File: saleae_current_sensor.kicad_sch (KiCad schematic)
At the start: 35 parts, among them J1 USB4505-03-0-A_REVA, J2 Conn_01x01_Female, J3 Conn_01x01_Female, J4 Conn_02x04_Counter_Clockwise, U1 TES_1-0523, U2 L78L12, U3 L7912, U4 ACS723xLCTR-05AB, U5 ACS723xLCTR-40AB, U6 AD8422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

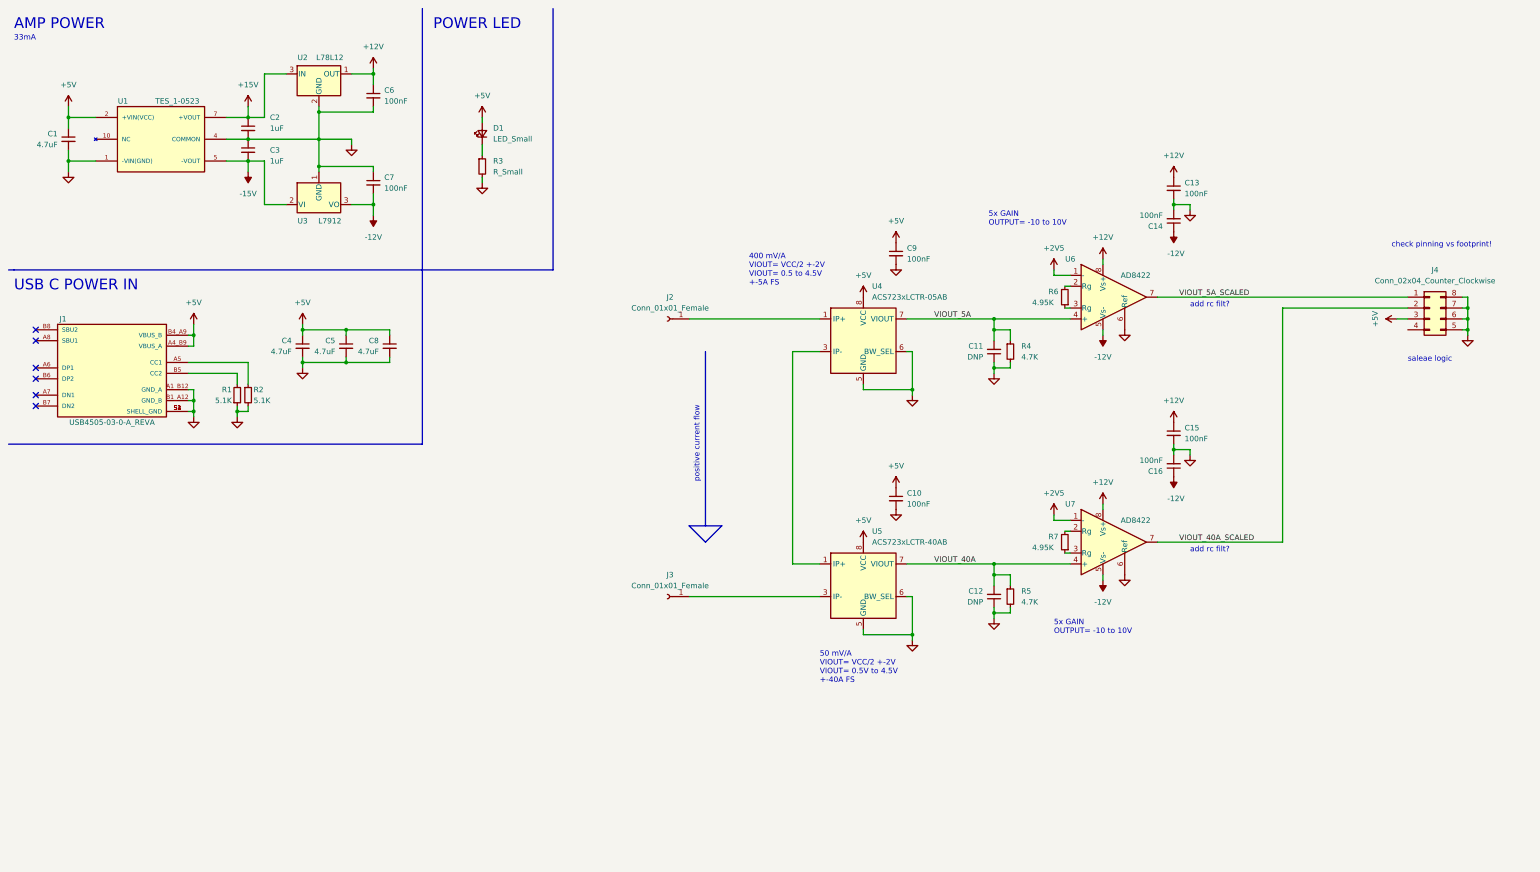
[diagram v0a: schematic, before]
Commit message: Add buffers to raw signals Add connections for main power lines Annotate all components Assign all footprints
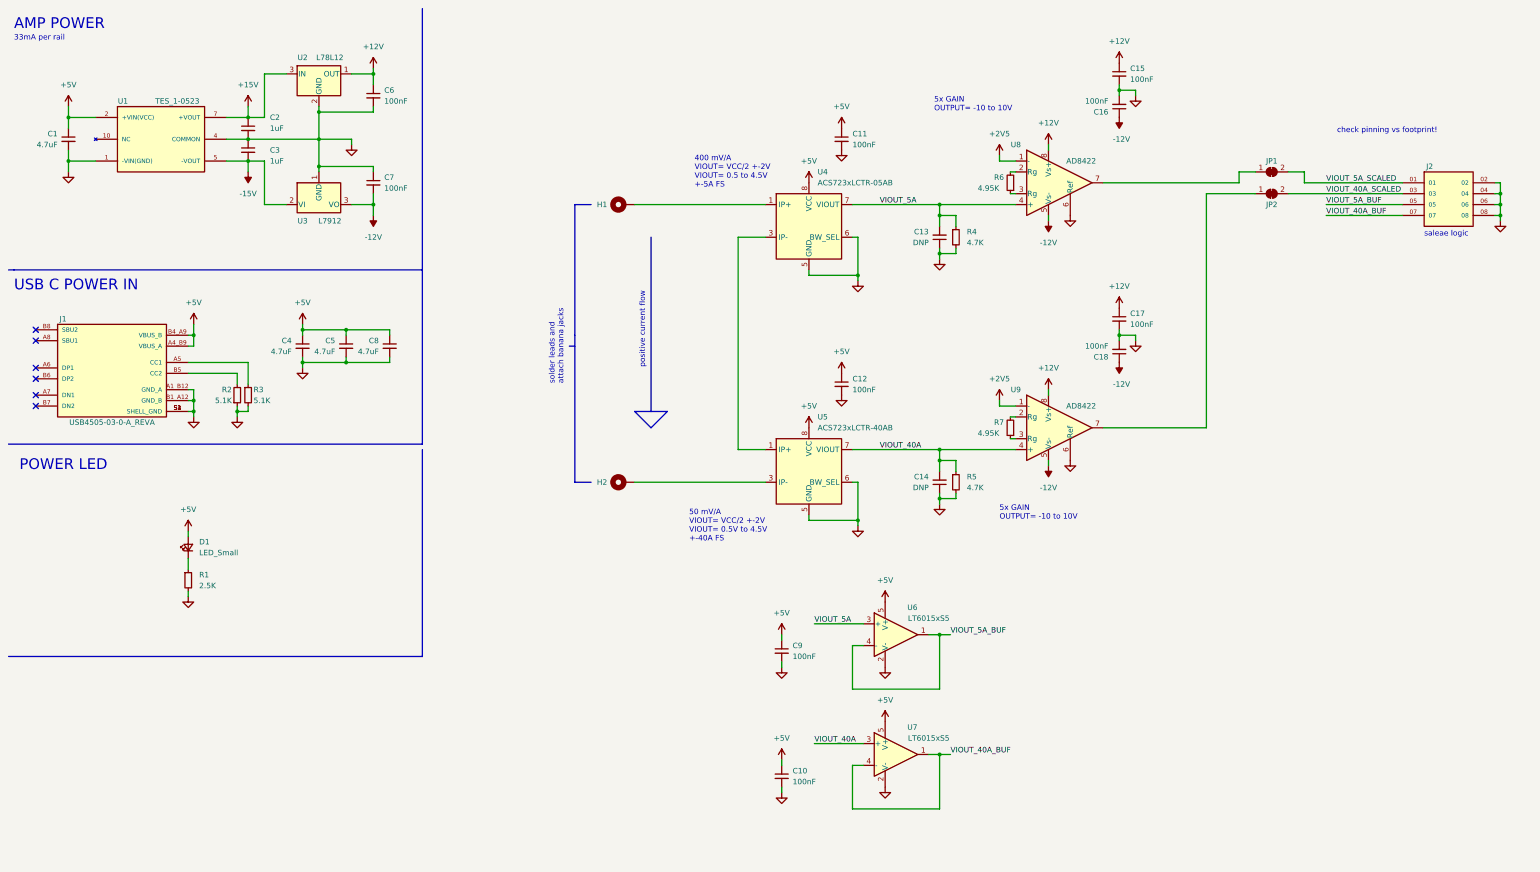
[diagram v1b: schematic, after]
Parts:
- removed J2, J3: Conn_01x01_Female, symbol Connector:Conn_01x01_Female
- removed J4: Conn_02x04_Counter_Clockwise, symbol Connector_Generic:Conn_02x04_Counter_Clockwise
- removed R3: R_Small, symbol Device:R_Small
- added C10, C9: 100nF, Capacitor_SMD:C_0603_1608Metric, symbol Device:C_Small
- added H1: IP, MountingHole:MountingHole_2.7mm_M2.5_ISO7380_Pad_TopBottom, symbol Mechanical:MountingHole_Pad
- added H2: IN, MountingHole:MountingHole_2.7mm_M2.5_ISO7380_Pad_TopBottom, symbol Mechanical:MountingHole_Pad
- added J2: FTSH-104-01-SM-D-RA, FTSH-104-01-SM-D-RA:SAMTEC_FTSH-104-01-SM-D-RA, symbol FTSH-104-01-SM-D-RA:FTSH-104-01-SM-D-RA
- added JP1, JP2: SolderJumper_2_Bridged, Jumper:SolderJumper-2_P1.3mm_Bridged2Bar_Pad1.0x1.5mm, symbol Jumper:SolderJumper_2_Bridged
- added R1: 2.5K, Resistor_SMD:R_0603_1608Metric, symbol Device:R_Small
- added U6, U7: LT6015xS5, Package_TO_SOT_SMD:SOT-23-5, symbol Amplifier_Operational:LT6015xS5
- C1, C2, C3, C4, C5, C8: footprint (none) -> Capacitor_SMD:C_1206_3216Metric
- C11: renamed from C9; footprint (none) -> Capacitor_SMD:C_0603_1608Metric
- C12: renamed from C10; footprint (none) -> Capacitor_SMD:C_0603_1608Metric
- C13: renamed from C11; footprint (none) -> Capacitor_SMD:C_0603_1608Metric
- C14: renamed from C12; footprint (none) -> Capacitor_SMD:C_0603_1608Metric
- C15: renamed from C13; footprint (none) -> Capacitor_SMD:C_0603_1608Metric
- C16: renamed from C14; footprint (none) -> Capacitor_SMD:C_0603_1608Metric
- C17: renamed from C15; footprint (none) -> Capacitor_SMD:C_0603_1608Metric
- C18: renamed from C16; footprint (none) -> Capacitor_SMD:C_0603_1608Metric
- C6, C7: footprint (none) -> Capacitor_SMD:C_0603_1608Metric
- D1: footprint (none) -> LED_SMD:LED_1206_3216Metric
- J1: footprint GCT_USB4505-03-0-A_REVA -> USB4505-03-0-A_REVA:GCT_USB4505-03-0-A_REVA
- R2: renamed from R1; footprint (none) -> Resistor_SMD:R_0603_1608Metric
- R3: renamed from R2; footprint (none) -> Resistor_SMD:R_0603_1608Metric
- R4, R5, R6, R7: footprint (none) -> Resistor_SMD:R_0603_1608Metric
- U1: footprint CONV_TES_1-0523 -> TES_1-0523:CONV_TES_1-0523
- U8: renamed from U6; footprint (none) -> AD8422BRMZ-RL:SOP65P490X110-8N
- U9: renamed from U7; footprint (none) -> AD8422BRMZ-RL:SOP65P490X110-8N
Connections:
- net +5V: now also C10.1, C9.1, U6.5 (V+), U7.5 (V+)
- net GND: now also C10.2, C9.2, J2.02, J2.04, J2.06, J2.08, R1.2, U6.2 (V-), U7.2 (V-)
- net VIOUT_40A: now also U7.3 (+)
- net VIOUT_40A_SCALED: now also J2.03, JP2.2 (B); no longer U9.7
- net VIOUT_5A: now also U6.3 (+)
- net VIOUT_5A_SCALED: now also J2.01, JP1.2 (B); no longer U8.7
- net at D1.1 (K): now also R1.1
- net at U4.1 (IP+), U4.2 (IP+): now also H1.1
- net at U5.3 (IP-), U5.4 (IP-): now also H2.1
- new net: JP2.1 (A), U9.7
- new net: JP1.1 (A), U8.7
- new net VIOUT_40A_BUF: J2.07, U7.1, U7.4 (-)
- new net VIOUT_5A_BUF: J2.05, U6.1, U6.4 (-)
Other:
- note added: "33mA per rail"
- note added: "solder leads and attach banana jacks"
- note removed: "33mA"
- note removed: "add rc filt?"
- moved on the sheet: C11, C12, C13, C14, C15, C16, C17, C18, R4, R5, R6, R7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

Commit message: Layout complete
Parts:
- removed J2: FTSH-104-01-SM-D-RA, FTSH-104-01-SM-D-RA:SAMTEC_FTSH-104-01-SM-D-RA, symbol FTSH-104-01-SM-D-RA:FTSH-104-01-SM-D-RA
- added J2: TSM-104-02-T-DH, TSM-104-02-T-DH:SAMTEC_TSM-104-02-T-DH, symbol TSM-104-02-T-DH:TSM-104-02-T-DH
- added M1, M2, M3: MountingHole_Pad, MountingHole:MountingHole_3.2mm_M3_ISO7380_Pad_TopBottom, symbol Mechanical:MountingHole_Pad
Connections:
- net GND: now also J2.01, J2.03, J2.05, J2.07, M1.1, M2.1, M3.1
- net VIOUT_40A_BUF: now also J2.02
- net VIOUT_40A_SCALED: now also J2.06
- net VIOUT_5A_BUF: now also J2.04
- net VIOUT_5A_SCALED: now also J2.08
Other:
- note added: "MOUNTING HOLES (M3)"
- note removed: "check pinning vs footprint!"
